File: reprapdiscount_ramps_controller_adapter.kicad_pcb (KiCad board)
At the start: 2 copper layers, 62.1 x 21.2 mm, 5 parts

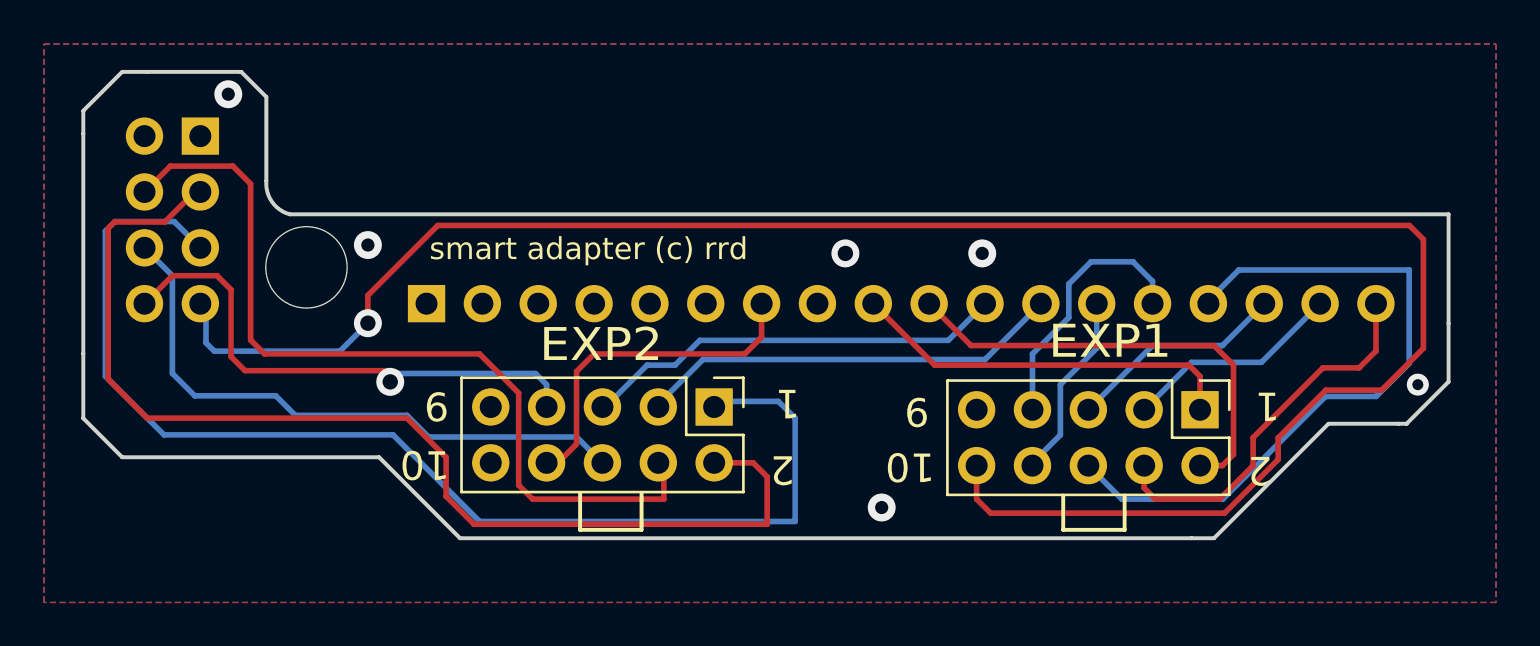
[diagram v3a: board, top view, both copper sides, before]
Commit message: adapter: add ldo connections
- adapter: update silkscreen
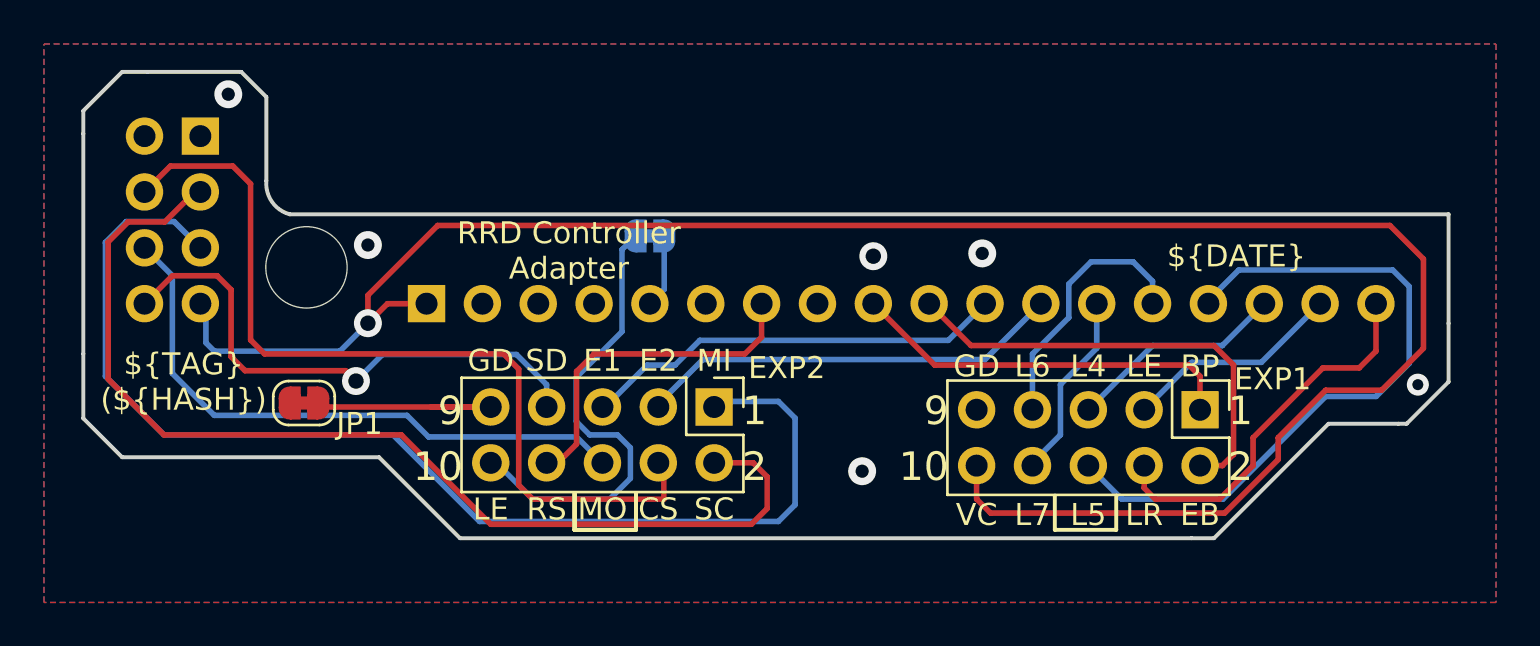
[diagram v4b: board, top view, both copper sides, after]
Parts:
- added JP1: Jumper_2_Bridged, Jumper:SolderJumper-2_P1.3mm_Bridged_RoundedPad1.0x1.5mm, F.Cu at (79.1, -58.6)
- added JP2: Jumper_2_Bridged, Jumper:SolderJumper-2_P1.3mm_Bridged_RoundedPad1.0x1.5mm, B.Cu at (94.9, -66.2)
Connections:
- AUX-4 pad 1: unconnected-(AUX-4-Pin_1-Pad1) -> VCC
- AUX-4 pad 2: unconnected-(AUX-4-Pin_2-Pad2) -> GND
- AUX-4 pad 5: unconnected-(AUX-4-Pin_5-Pad5) -> Net-(AUX-4-Pin_5)
- EXP2 pad 10: B10 -> PWR_LED
- EXP2 pad 9: B9 -> Net-(JP1-A)
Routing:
- net PWR_LED: track 0.00 -> 21.3 mm
- net Net-(JP1-A): track 0.00 -> 10.6 mm
- net Net-(AUX-4-Pin_5): track 0.00 -> 3.39 mm
- net VCC: track 91.5 -> 94.0 mm
- net HOST_SCK: track 50.3 -> 48.5 mm
- net SD_MISO: track 54.5 -> 53.8 mm
- net HOST_CS: track 38.8 -> 39.4 mm
- net GND: vias 5 -> 6
- net (no net): vias 1 -> 0
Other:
- board text added: "${DATE}"
- board text added: "${TAG} (${HASH})"
- board text added: "7"
- board text added: "8"
- board text added: "BP"
- board text added: "CS"
- board text added: "D32"
- board text added: "D39"
- board text added: "D43"
- board text added: "D47"
- board text added: "E1"
- board text added: "E2"
- board text added: "EB"
- board text added: "GD"
- board text added: "JLCJLCJLCJLC"
- board text added: "L4"
- board text added: "L5"
- board text added: "L6"
- board text added: "L7"
- board text added: "LE"
- board text added: "LR"
- board text added: "MI"
- board text added: "MO"
- board text added: "NC"
- board text added: "RRD Controller Adapter"
- board text added: "RS"
- board text added: "SC"
- board text added: "SD"
- board text added: "VC"
- board text removed: "smart adapter (c) rrd"
